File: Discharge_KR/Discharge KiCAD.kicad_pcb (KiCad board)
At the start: 2 copper layers, 79.9 x 54.6 mm, 17 parts, among them IC1 AL5890-10D-13, J1 Conn_01x02, J2 Conn_01x02, J3 Conn_01x02, J4 Conn_01x03, K1 DBR71210, Q1 2N7000, U2 HCPL-817-000E

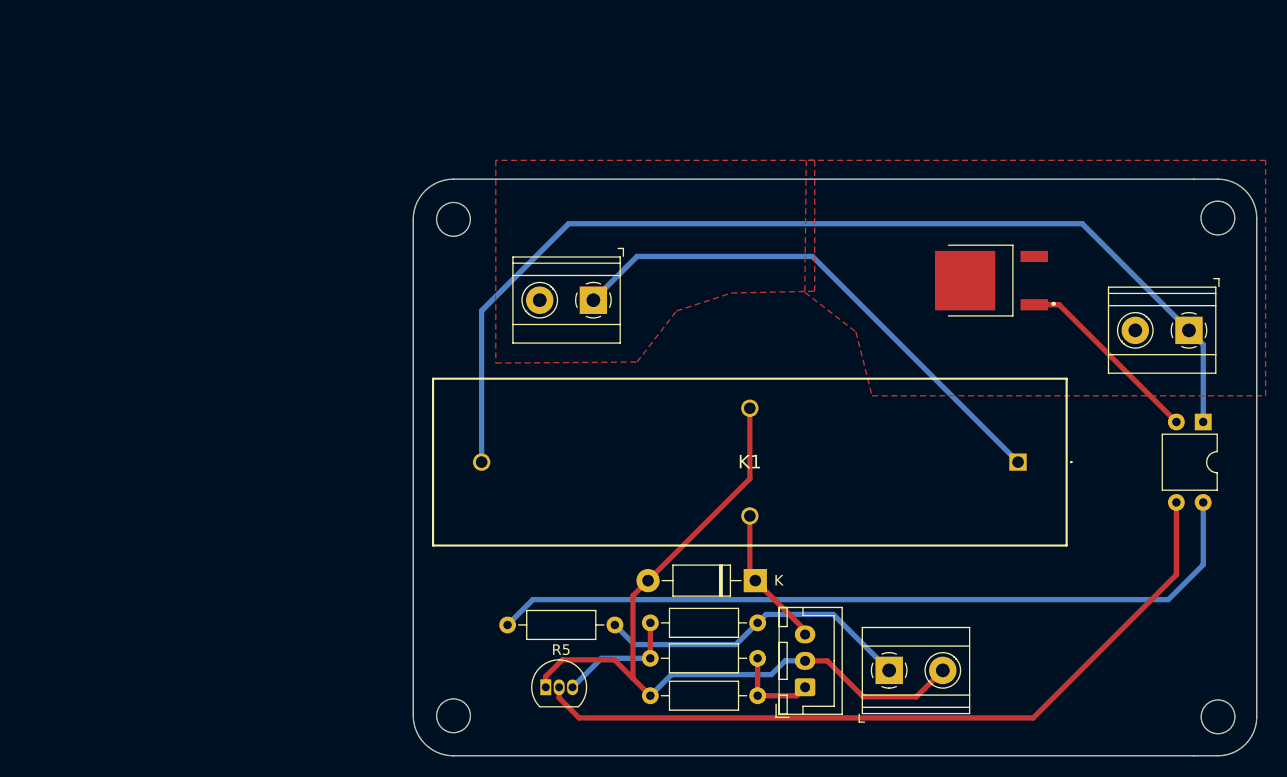
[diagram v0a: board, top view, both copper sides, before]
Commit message: precharge and discharge fixed
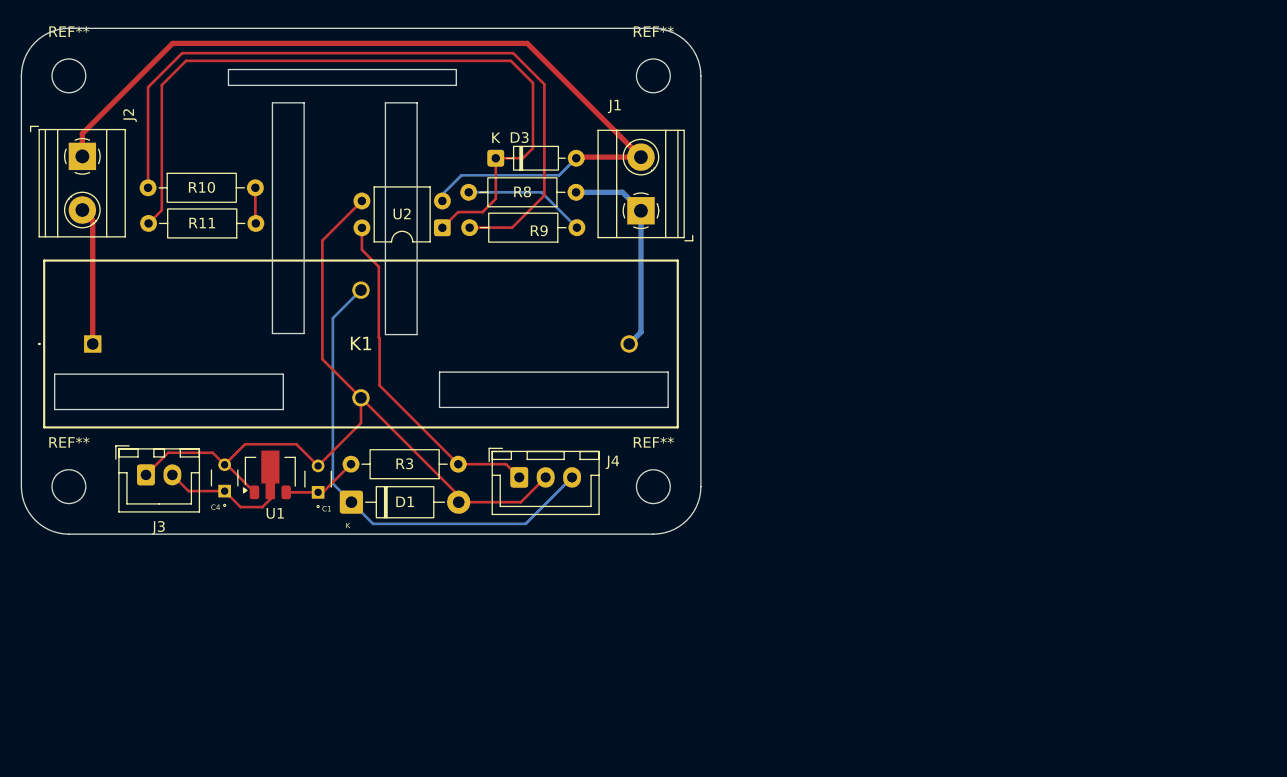
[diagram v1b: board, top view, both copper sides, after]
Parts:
- removed H1, H2, H3 (x2): M3, MountingHole:MountingHole_3.2mm_M3
- removed IC1: AL5890-10D-13, AL5890_10_D13:AL589010D13
- removed Q1: 2N7000, Package_TO_SOT_THT:TO-92_Inline
- removed R2, R5: 1k, Resistor_THT:R_Axial_DIN0207_L6.3mm_D2.5mm_P10.16mm_Horizontal
- removed R4: 3.3k, Resistor_THT:R_Axial_DIN0207_L6.3mm_D2.5mm_P10.16mm_Horizontal
- added C1: 1uF, FA14_Capacitor:FA18X7R1H104KNU00, F.Cu at (117.0, 98.2)
- added C4: 1uF, FA14_Capacitor:FA18X7R1H104KNU00, F.Cu at (108.1, 98.1)
- added D3: 1N4148, Diode_THT:D_DO-35_SOD27_P7.62mm_Horizontal, F.Cu at (133.8, 66.6)
- added R10: 56k, Resistor_THT:R_Axial_DIN0207_L6.3mm_D2.5mm_P10.16mm_Horizontal, F.Cu at (100.9, 69.4)
- added R11: 56k, Resistor_THT:R_Axial_DIN0207_L6.3mm_D2.5mm_P10.16mm_Horizontal, F.Cu at (111.1, 72.8)
- added R8: 56k, Resistor_THT:R_Axial_DIN0207_L6.3mm_D2.5mm_P10.16mm_Horizontal, F.Cu at (141.4, 69.8)
- added R9: 56k, Resistor_THT:R_Axial_DIN0207_L6.3mm_D2.5mm_P10.16mm_Horizontal, F.Cu at (141.5, 73.2)
- added REF**: MountingHole_3.2mm_M3, MountingHole:MountingHole_3.2mm_M3, F.Cu at (93.4, 58.8)
- added REF**: MountingHole_3.2mm_M3, MountingHole:MountingHole_3.2mm_M3, F.Cu at (148.7, 58.8)
- added REF**: MountingHole_3.2mm_M3, MountingHole:MountingHole_3.2mm_M3, F.Cu at (93.4, 97.7)
- added REF**: MountingHole_3.2mm_M3, MountingHole:MountingHole_3.2mm_M3, F.Cu at (148.7, 97.7)
- added U1: MCP1703AT-3302E/MBVAO, Package_TO_SOT_SMD:SOT-89-3, F.Cu at (112.5, 96.3)
- J3: footprint Phoenix 1x2 Connector:Phoenix_1x2_1729128 -> Connector_JST:JST_XH_B2B-XH-A_1x02_P2.50mm_Vertical
- R3: value 8.2k -> 10k
- moved K1 88.3 mm to (95.6, 84.2), turned to 0 degrees
- moved U2 74.4 mm to (128.7, 73.2), turned to 180 degrees
- moved J3 72.8 mm to (100.7, 96.6)
- moved J1 53.1 mm to (147.6, 71.6), turned to 90 degrees
- moved J2 50.3 mm to (94.7, 66.4), turned to -90 degrees
- moved D1 39.0 mm to (120.1, 99.2), turned to 0 degrees
- moved J4 33.6 mm to (136.0, 96.8), turned to 0 degrees
- moved R3 25.9 mm to (130.2, 95.6), turned to 180 degrees
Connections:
- J2 pad 1: TS+ -> TS-
- J2 pad 2: TS- -> TS+
- J3 pad 1: GLV+ -> GLV-
- J3 pad 2: GLV- -> GLV+
- J4 pad 1: ~{DISCHARGING} -> Discharing_N
- R3 pad 1: Net-(Q1-D) -> Discharing_N
- R3 pad 2: ~{DISCHARGING} -> 3.3V
- U2 pad 1: Net-(J1-Pin_1) -> Net-(D3-K)
- U2 pad 2: Net-(IC1-IN) -> TS-
- U2 pad 3: Net-(Q1-G) -> GLV-
- U2 pad 4: Net-(R5-Pad2) -> Discharing_N
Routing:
- net TS-: track 0.00 -> 84.1 mm
- net Net-(J1-Pin_1): track 98.2 -> 20.0 mm
- net Net-(R5-Pad2): track 74.1 -> 0.00 mm
- net Net-(Q1-G): track 72.7 -> 0.00 mm
- net Net-(D3-K): track 0.00 -> 70.7 mm
- net Net-(R10-Pad1): track 0.00 -> 68.5 mm
- net TS+: track 50.0 -> 13.1 mm
- net Discharing_N: track 0.00 -> 32.5 mm
- net SDWN_DC+: track 13.4 -> 45.5 mm
- net GLV+: track 30.1 -> 11.6 mm
- net Net-(IC1-IN): track 18.1 -> 0.00 mm
- net Net-(Q1-D): track 11.9 -> 0.00 mm
- net Net-(R8-Pad2): track 0.00 -> 11.6 mm
- net ~{DISCHARGING}: track 8.37 -> 0.00 mm
- net 3.3V: track 0.00 -> 7.24 mm
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- removed copper zone on F.Cu, net TS-
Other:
- board size 79.9 x 54.6 mm -> 64.3 x 47.9 mm

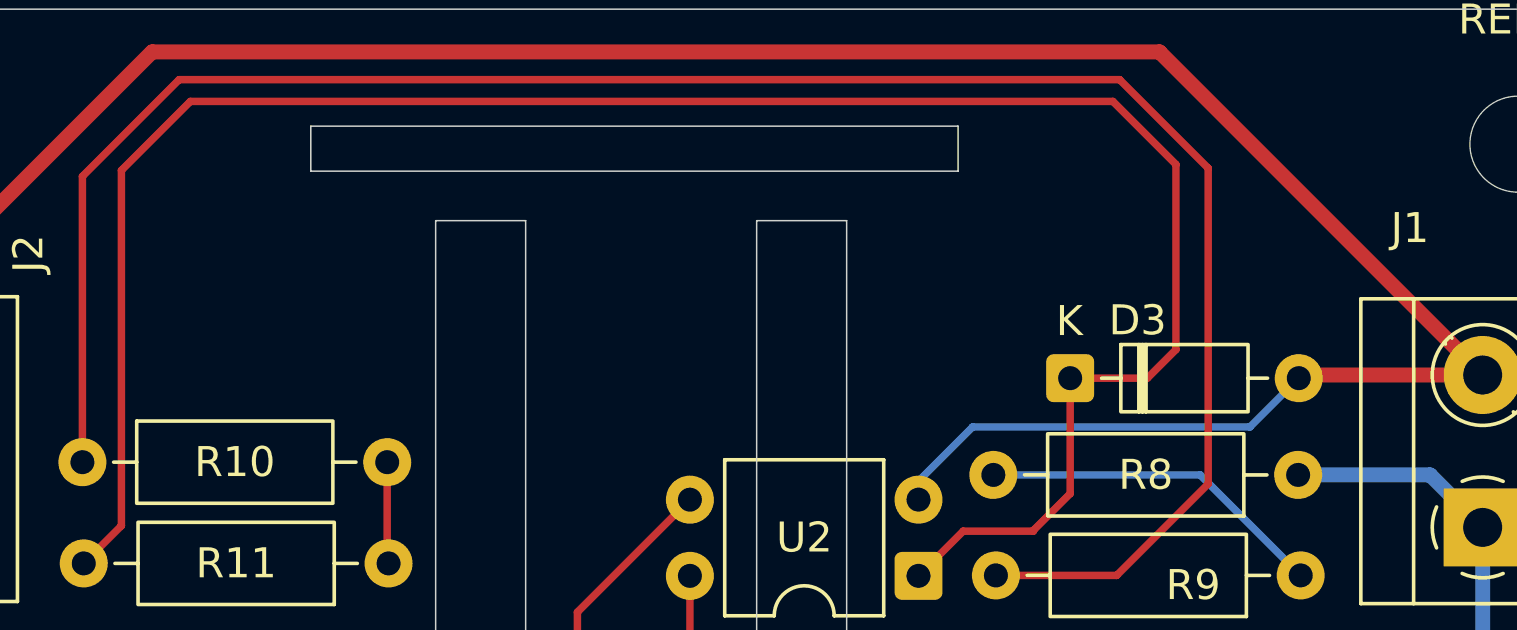
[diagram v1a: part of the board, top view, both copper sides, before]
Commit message: Voltage measurement completed
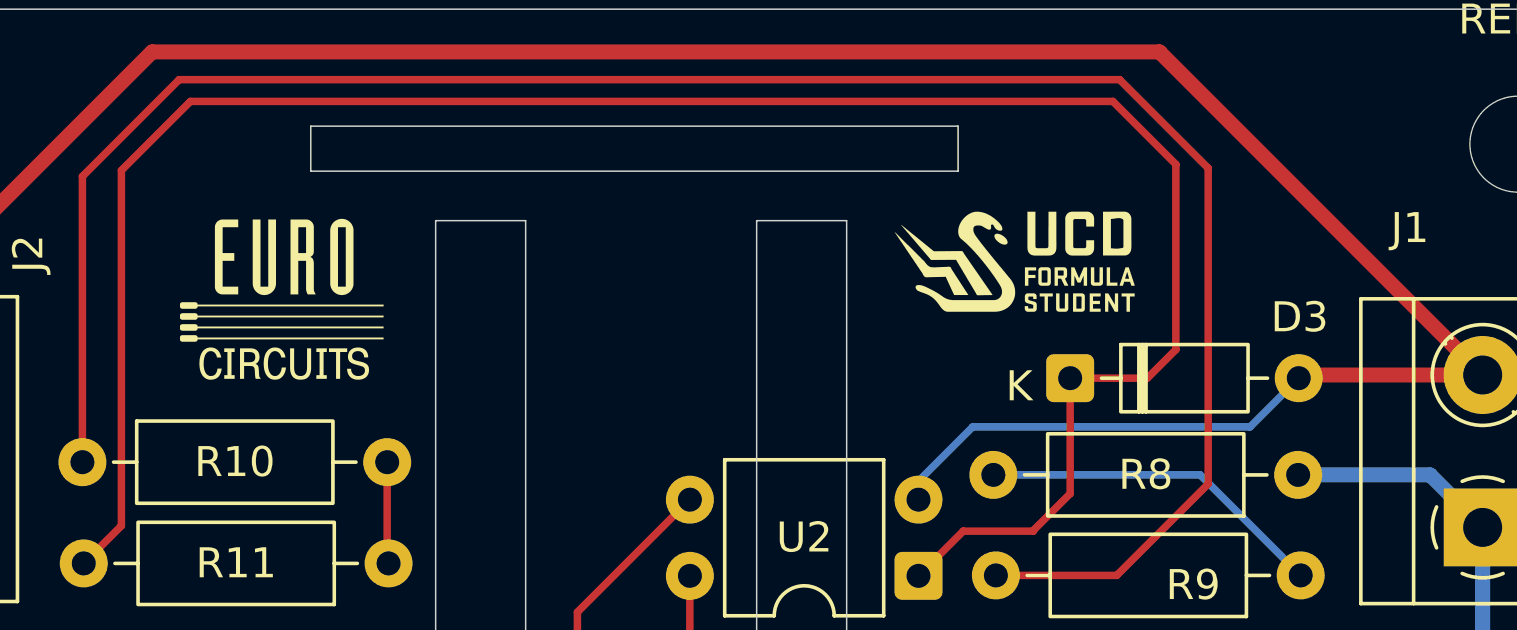
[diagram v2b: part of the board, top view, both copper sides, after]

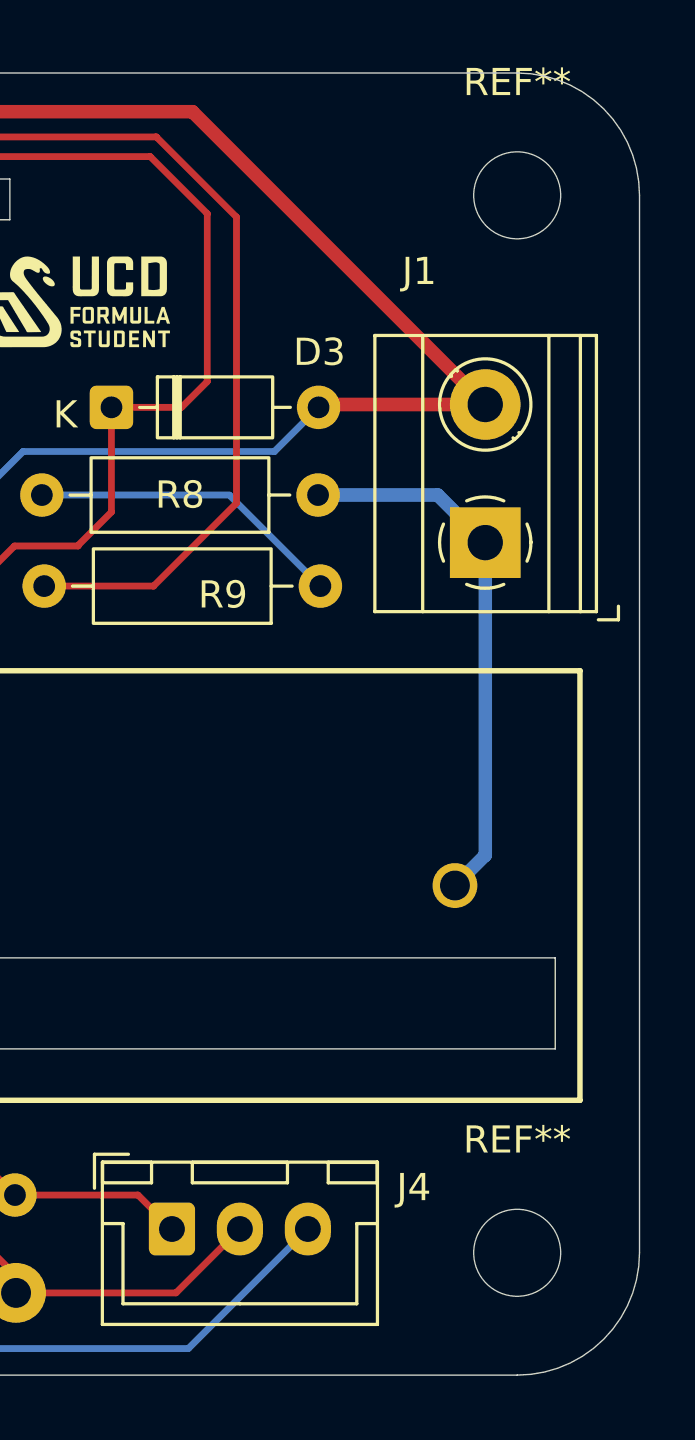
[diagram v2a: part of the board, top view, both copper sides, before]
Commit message: added HVLV labels
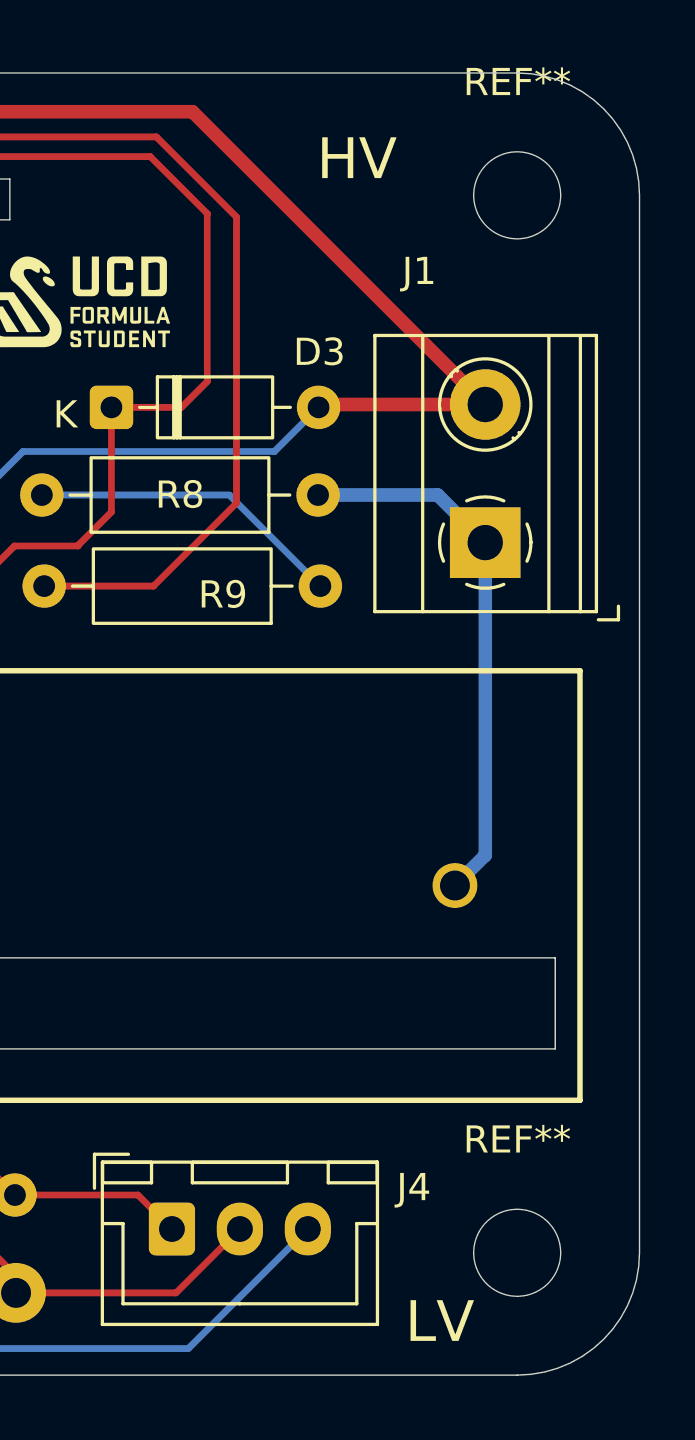
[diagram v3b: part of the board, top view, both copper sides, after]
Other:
- board text added: "HV"
- board text added: "LV"
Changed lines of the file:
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@@
 		(layer "Edge.Cuts")
+	)
+	(gr_text "HV"
+		(at 141.35 58.35 0)
+		(layer "F.SilkS")
+		(effects
+			(font
+				(size 1.5 1.5)
+				(thickness 0.15)
+			)
+			(justify left bottom)
+		)
+	)
+	(gr_text "LV"
+		(at 144.6 101.125 0)
+		(layer "F.SilkS")
+		(effects
+			(font
+				(size 1.5 1.5)
+				(thickness 0.15)
+			)
+			(justify left bottom)
+		)
 	)
 	(segment

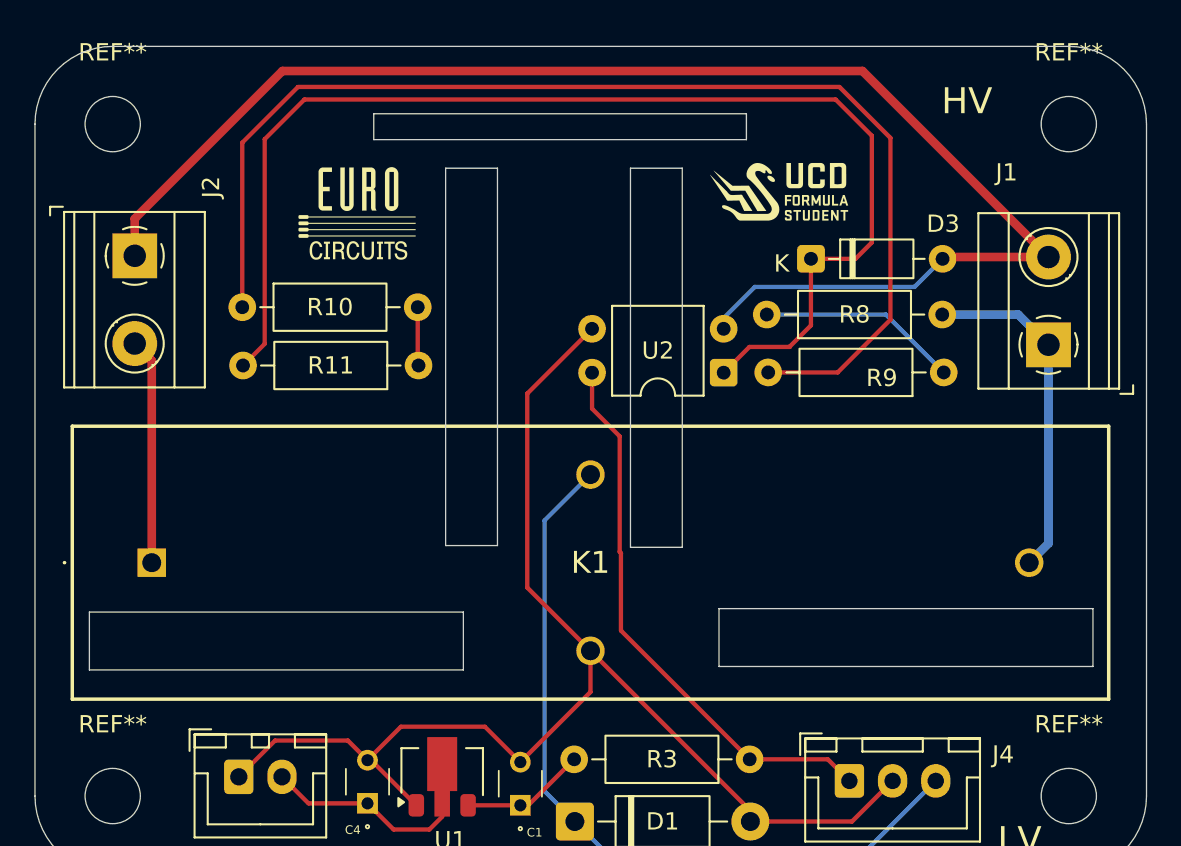
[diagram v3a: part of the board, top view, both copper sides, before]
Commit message: slave with new fuses added
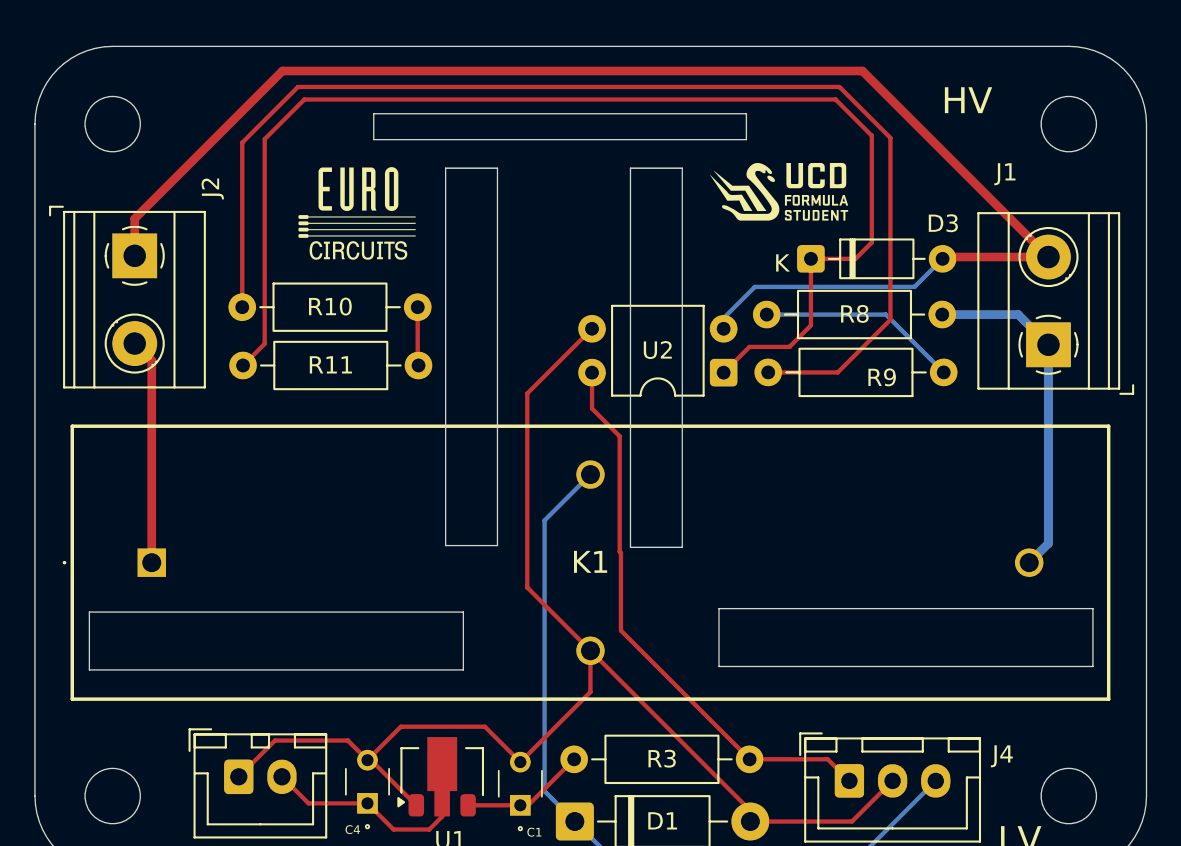
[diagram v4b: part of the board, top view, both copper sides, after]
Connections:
- net Discharing_N renamed Discharging_N
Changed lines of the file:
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@@
 	(net 7 "Net-(J1-Pin_1)")
 	(net 8 "TS+")
-	(net 9 "Discharing_N")
+	(net 9 "Discharging_N")
 	(net 10 "Net-(R8-Pad2)")
 	(net 11 "Net-(R10-Pad1)")
@@
 			(layers "*.Cu" "*.Mask")
 			(remove_unused_layers no)
-			(net 9 "Discharing_N")
+			(net 9 "Discharging_N")
 			(pintype "passive")
 		)
@@
 			(at 0 -4.15 0)
 			(layer "F.SilkS")
+			(hide yes)
 			(effects
 				(font
@@
 			(layers "*.Cu" "*.Mask")
 			(remove_unused_layers no)
-			(net 9 "Discharing_N")
+			(net 9 "Discharging_N")
 			(pintype "passive")
 		)
@@
 			(at 0 -4.15 0)
 			(layer "F.SilkS")
+			(hide yes)
 			(effects
 				(font
@@
 			(at 0 -4.15 0)
 			(layer "F.SilkS")
+			(hide yes)
 			(effects
 				(font
@@
 			(at 0 -4.15 0)
 			(layer "F.SilkS")
+			(hide yes)
 			(effects
 				(font
@@
 			(remove_unused_layers no)
 			(roundrect_rratio 0.147059)
-			(net 9 "Discharing_N")
+			(net 9 "Discharging_N")
 			(pinfunction "Pin_1")
 			(pintype "passive")
